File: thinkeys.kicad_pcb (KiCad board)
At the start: 2 copper layers, 363.7 x 279.2 mm, 692 parts, among them J1 Pointing stick, J2 Pointing stick, J3 PWRSWITCH, SW1 SW_Push, SW10 SW_Push, SW11 SW_Push, SW12 SW_Push, SW13 SW_Push, SW14 SW_Push, SW15 SW_Push, SW16 SW_Push, SW17 SW_Push, SW18 SW_Push, SW19 SW_Push, SW2 SW_Push, SW20 SW_Push, SW21 SW_Push, SW22 SW_Push, SW23 SW_Push, SW24 SW_Push, SW25 SW_Push, SW26 SW_Push, SW27 SW_Push, SW28 SW_Push, SW29 SW_Push, SW3 SW_Push, SW30 SW_Push, SW31 SW_Push, SW32 SW_Push, SW33 SW_Push, SW34 SW_Push, SW35 SW_Push, SW36 SW_Push, SW37 SW_Push, SW38 SW_Push, SW39 SW_Push, SW4 SW_Push, SW40 SW_Push, SW41 SW_Push, SW42 SW_Push, SW43 SW_Push, SW44 SW_Push, SW45 SW_Push, SW46 SW_Push, SW47 SW_Push, SW48 SW_Push, SW49 SW_Push, SW5 SW_Push, SW50 SW_Push, SW51 SW_Push, SW52 SW_Push, SW53 SW_Push, SW54 SW_Push, SW55 SW_Push, SW56 SW_Push, SW57 SW_Push, SW58 SW_Push, SW59 SW_Push, SW6 SW_Push, SW60 SW_Push, SW61 SW_Push, SW62 SW_Push, SW63 SW_Push, SW64 SW_Push, SW65 SW_Push, SW66 SW_Push, SW67 SW_Push, SW68 SW_Push, SW69 SW_Push, SW7 SW_Push, SW70 SW_Push, SW71 SW_Push, SW72 SW_Push, SW73 SW_Push, SW74 SW_Push, SW75 SW_Push, SW76 SW_Push, SW77 SW_Push, SW78 SW_Push, SW79 SW_Push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

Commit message: oled btfo
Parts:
- removed OL1, OL2: OLED, libmodulo:128x64OLED

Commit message: switch to matching flush top pad for bottom hole
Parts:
- TP1, TP13, TP14, TP15, TP16, TP17, TP18, TP2, TP25, TP26, TP27, TP28, TP29, TP3, TP30, TP31, TP39, TP4, TP40, TP41, TP42, TP43, TP44, TP45, TP46, TP5, TP55, TP56, TP57, TP58, TP59, TP6, TP65, TP66, TP67, TP68, TP69: footprint libmodulo:TestPoint_Keystone_5019_Minature -> libmodulo:SMDPad_4.0x2.0mm
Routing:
- net /left/c5: track 73.1 -> 75.6 mm
- net /right/r3: track 68.1 -> 70.7 mm
- net /right/c3: track 107.3 -> 109.9 mm
- net /right/c0: track 72.1 -> 74.7 mm
- net /left/r4: track 41.2 -> 43.7 mm
- net /left/r1: track 48.8 -> 51.3 mm
- net /left/c2: track 98.4 -> 101.0 mm
- net /right/c6: track 131.3 -> 133.8 mm
- net VDD: track 64.8 -> 66.0 mm
- net /right/r0: track 161.2 -> 162.5 mm
- net /right/c4: track 115.3 -> 116.6 mm
- net /right/c2: track 96.4 -> 97.6 mm
- net /left/r0: track 135.5 -> 136.8 mm
- net /left/c4: track 79.2 -> 80.5 mm
- net /left/r5: track 38.9 -> 40.1 mm
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
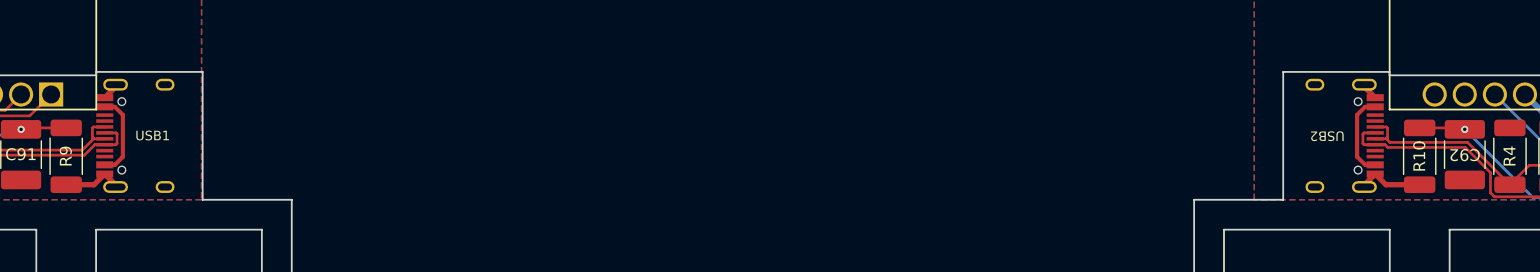
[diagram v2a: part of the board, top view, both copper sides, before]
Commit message: pcb: fix split connection usb location
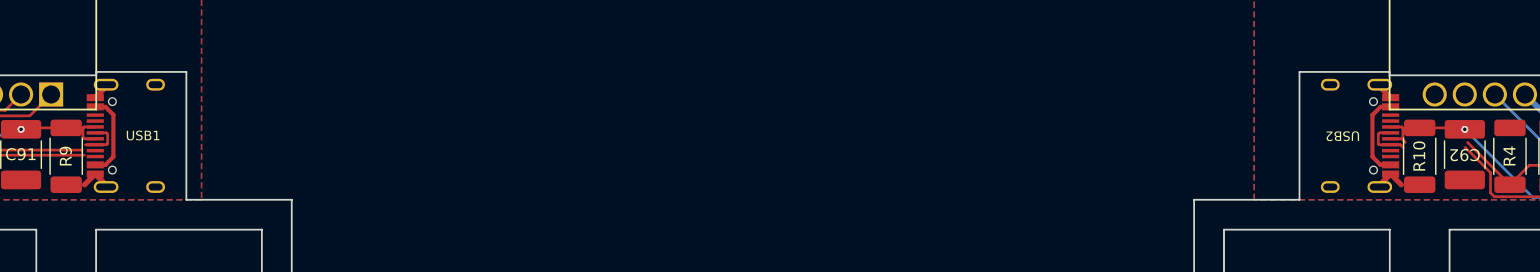
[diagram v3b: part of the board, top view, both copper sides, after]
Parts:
- moved USB2 1.30 mm to (208.9, -14.9)
- moved USB1 0.80 mm to (114.9, -14.9)
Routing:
- net /right/SCL: track 81.1 -> 74.5 mm
- net /right/SDA: track 87.1 -> 80.5 mm
- net GND2: track 49.9 -> 47.0 mm
- net GND1: track 87.9 -> 86.2 mm
- net /left/SDA: track 64.5 -> 63.2 mm
- net /left/SCL: track 57.1 -> 55.8 mm
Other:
- outline, holes or cut-outs redrawn

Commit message: redo top positions, routing & footprints
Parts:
- C91, C92: value 2.2u -> 2.2µ; footprint libmodulo:C_1812_4532Metric_Pad1.57x3.40mm_HandSolder -> Capacitor_SMD:C_1812_4532Metric_Pad1.57x3.40mm_HandSolder
- R1, R10, R2, R3, R4, R5, R6, R7, R8, R9: footprint libmodulo:R_2010_5025Metric_Pad1.40x2.65mm_HandSolder -> Resistor_SMD:R_2010_5025Metric_Pad1.40x2.65mm_HandSolder
- SW91, SW92, SW93: footprint Button_Switch_SMD:SW_SPST_TL3305A -> Button_Switch_SMD:SW_SPST_EVQQ2
- moved SW93 42.8 mm to (286.6, -47.0), turned to 180 degrees
- moved JP2 35.3 mm to (251.5, -48.3), turned to 270 degrees
- moved SW92 15.9 mm to (238.1, -12.7), turned to 180 degrees
- moved SW91 15.3 mm to (85.7, -12.7), turned to 180 degrees
- moved JP1 14.2 mm to (72.4, -13.3), turned to 270 degrees
- moved R3 3.84 mm to (75.6, -12.7)
- moved R1 3.21 mm to (78.7, -12.7)
- moved J3 2.54 mm to (217.8, -33.7)
- moved U1 2.54 mm to (87.0, -26.0)
- moved U2 2.54 mm to (236.9, -26.0)
- moved C91 1.42 mm to (99.7, -12.7)
- moved C92 1.42 mm to (224.2, -12.7), turned to 90 degrees
- moved R10 1.36 mm to (220.3, -12.7), turned to 90 degrees
- moved R4 1.36 mm to (228.0, -12.7)
- moved R9 1.36 mm to (103.5, -12.7)
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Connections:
- U2 pad 1: /right/c7 -> Net-(JP2-Pad3)
- U2 pad 10: /right/c3 -> /right/c4
- U2 pad 11: /right/c2 -> /right/c3
- U2 pad 12: /right/c1 -> /right/c2
- U2 pad 13: /right/c0 -> /right/c1
- U2 pad 14: /right/r1 -> /right/c0
- U2 pad 15: /right/r2 -> /right/r1
- U2 pad 16: Net-(JP2-Pad1) -> /right/r2
- U2 pad 26: Net-(JP2-Pad3) -> Net-(JP2-Pad1)
- U2 pad 7: /right/c6 -> /right/c7
- U2 pad 8: /right/c5 -> /right/c6
- U2 pad 9: /right/c4 -> /right/c5
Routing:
- net Net-(J3-Pad1): track 73.9 -> 0.00 mm
- net GND1: track 86.2 -> 20.3 mm
- net /right/SDA: track 80.5 -> 22.6 mm
- net /right/SCL: track 74.5 -> 18.2 mm
- net /right/DATA: track 72.9 -> 17.2 mm
- net VDD: track 66.0 -> 115.7 mm
- net /left/SDA: track 63.2 -> 16.4 mm
- net Net-(JP1-Pad1): track 18.5 -> 59.9 mm
- net /left/SCL: track 55.8 -> 17.0 mm
- net /right/CLK: track 51.1 -> 25.8 mm
- net /right/RST: track 40.4 -> 15.1 mm, vias 1 -> 0
- net /right/r0: track 162.5 -> 137.6 mm, vias 1 -> 0
- net GND2: track 47.0 -> 24.0 mm, vias 1 -> 0
- net Net-(JP2-Pad3): track 23.0 -> 0.00 mm
- net /right/c7: track 153.7 -> 134.9 mm
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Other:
- outline, holes or cut-outs redrawn

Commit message: pcb: finish routing new top area
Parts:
- JP1, JP2: footprint libmodulo:SolderJumper-3_P1.3mm_Open_RoundedPad1.0x1.5mm_NumberLabels -> Jumper:SolderJumper-3_P1.3mm_Open_RoundedPad1.0x1.5mm_NumberLabels
- moved SW93 45.2 mm to (257.2, -12.7), turned to 0 degrees
- moved JP2 30.2 mm to (255.9, -18.4)
- moved R10 4.44 mm to (224.8, -12.7)
- moved R9 4.44 mm to (99.1, -12.7)
- moved C91 3.18 mm to (102.9, -12.7)
- moved C92 3.18 mm to (221.0, -12.7)
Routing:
- net Net-(J3-Pad1): track 0.00 -> 108.9 mm
- net GND1: track 20.3 -> 100.5 mm
- net /right/DATA: track 17.2 -> 95.4 mm
- net /right/SDA: track 22.6 -> 85.3 mm
- net GND2: track 24.0 -> 86.5 mm, vias 0 -> 1
- net /right/SCL: track 18.2 -> 80.1 mm
- net Net-(JP2-Pad3): track 0.00 -> 52.3 mm
- net VCC: track 68.7 -> 105.2 mm
- net /left/RST: track 40.7 -> 75.7 mm
- net /left/SCL: track 17.0 -> 50.2 mm
- net /right/CLK: track 25.8 -> 58.2 mm
- net /left/SDA: track 16.4 -> 45.3 mm
- net /right/r0: track 137.6 -> 161.2 mm, vias 0 -> 1
- net Net-(JP1-Pad3): track 1.89 -> 13.6 mm
- net Net-(JP2-Pad1): track 0.00 -> 11.1 mm, vias 0 -> 1
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
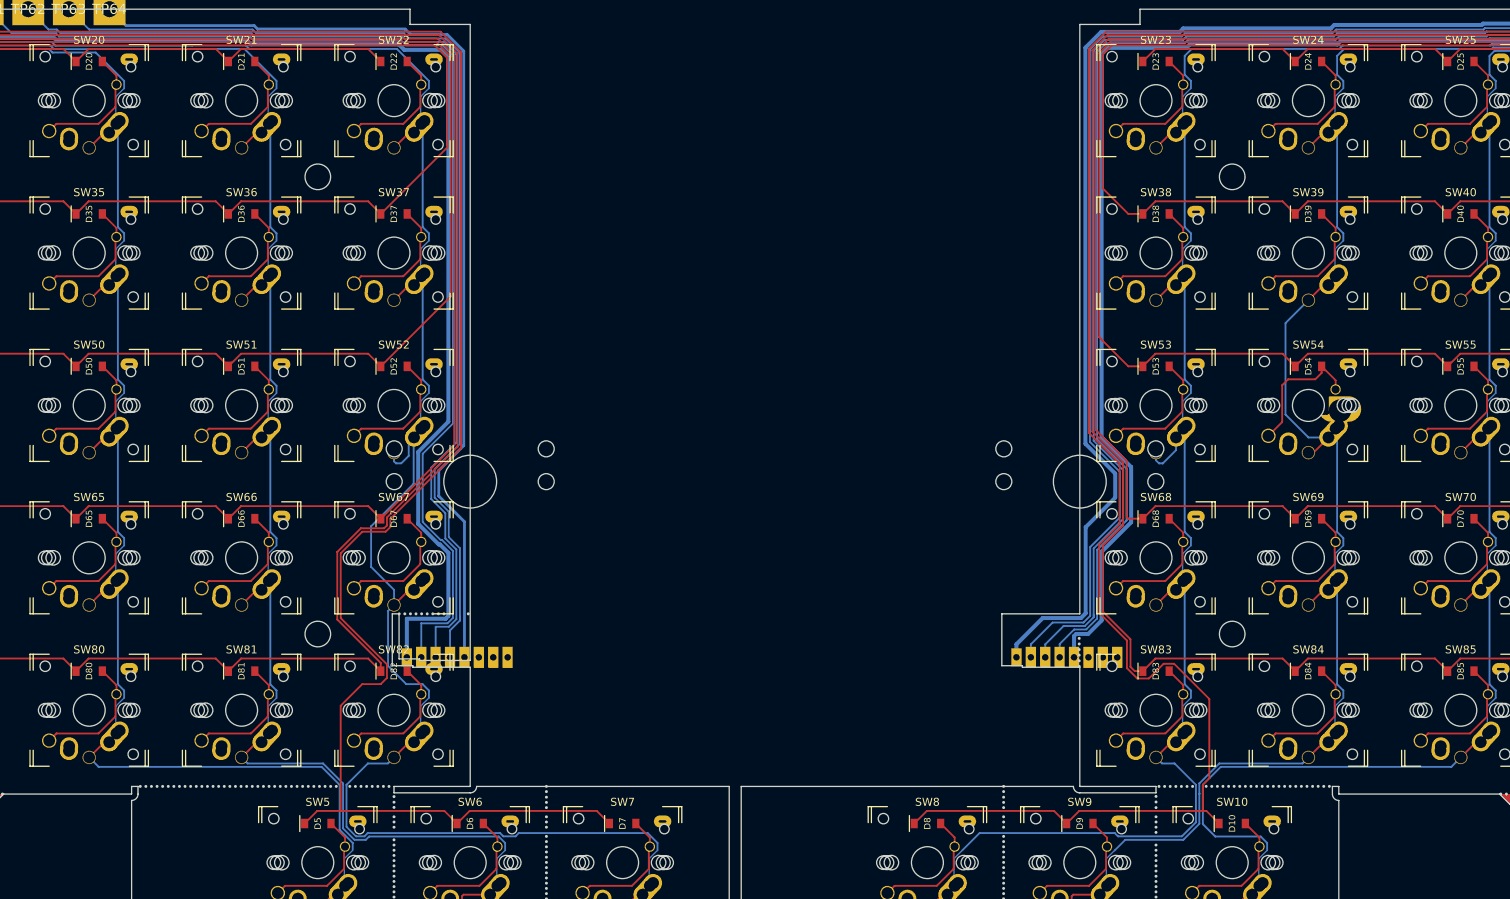
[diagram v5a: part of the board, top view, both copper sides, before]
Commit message: pcb: add magnetic tenting kit support
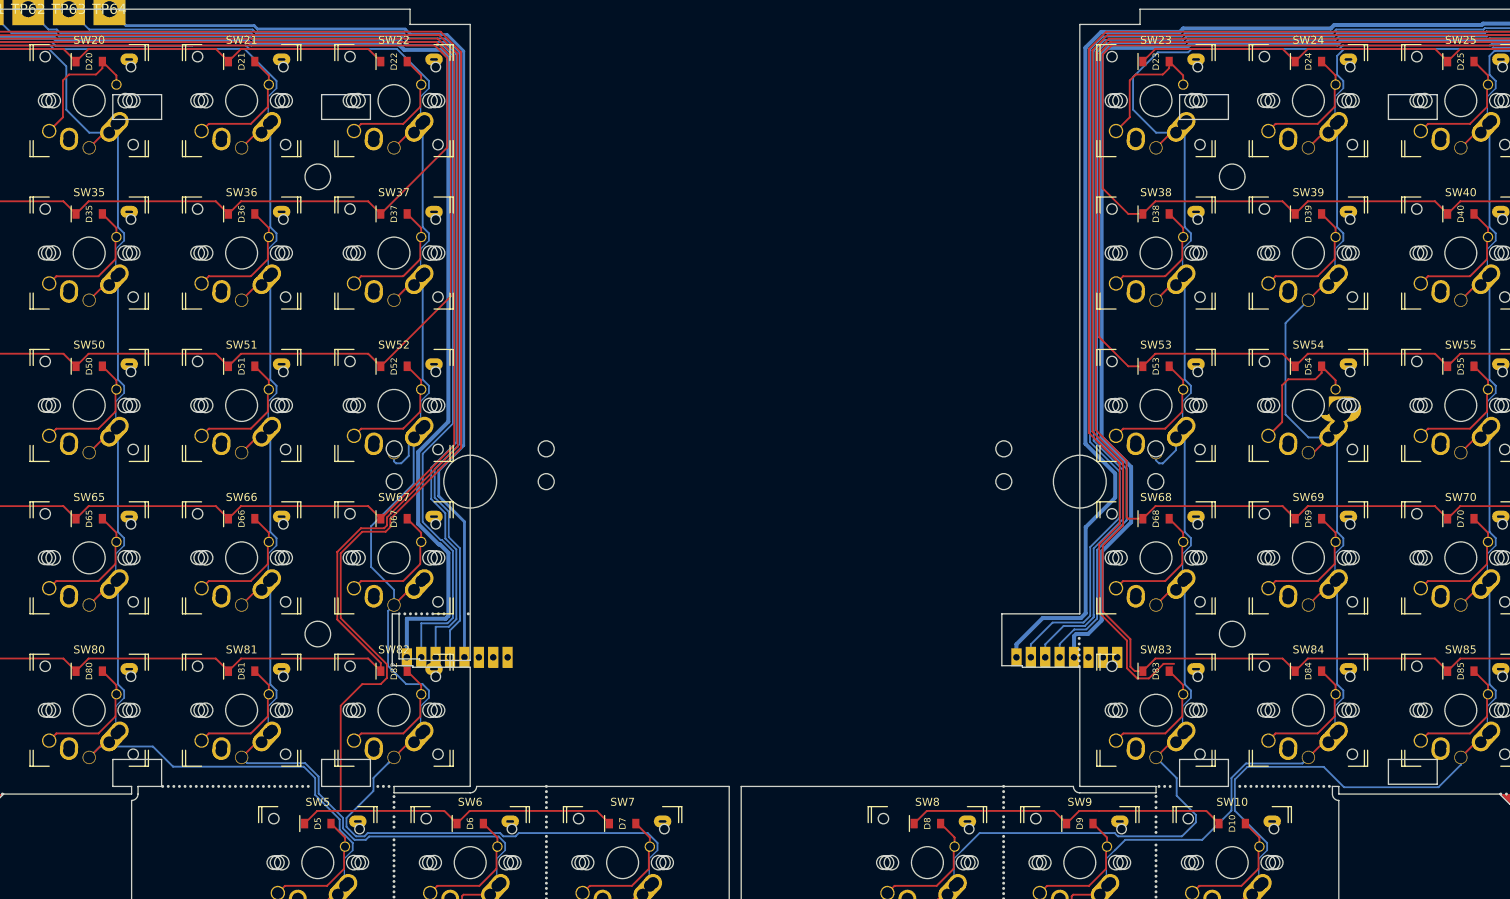
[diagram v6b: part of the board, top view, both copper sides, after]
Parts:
- removed the ? at (84.7, 219.1)
- removed the ? at (83.3, 219.1)
- removed the ? at (107.1, 219.1)
- removed the ? at (109.5, 219.1)
- removed the ? at (110.2, 219.1)
- removed the ? at (219.3, 219.1)
- removed the ? at (217.9, 219.1)
- removed the ? at (108.8, 219.1)
- removed the ? at (217.2, 219.1)
- removed the ? at (110.9, 219.1)
- removed the ? at (218.6, 219.1)
- removed the ? at (104.3, 219.1)
- removed the ? at (111.6, 219.1)
- removed the ? at (105.7, 219.1)
- removed the ? at (105.0, 219.1)
- removed the ? at (84.0, 219.1)
- removed the ? at (216.5, 219.1)
- removed the ? at (215.8, 219.1)
- removed the ? at (212.7, 219.1)
- removed the ? at (213.4, 219.1)
- removed the ? at (214.1, 219.1)
- removed the ? at (212.0, 219.1)
- removed the ? at (82.6, 219.1)
- removed the ? at (106.4, 219.1)
- added REF**: Magnetic Tenting Kit, libmodulo:Magnetic_Tenting_Kit, F.Cu at (228.6, 175.7)
- added REF**: Magnetic Tenting Kit, libmodulo:Magnetic_Tenting_Kit, F.Cu at (95.2, 175.7)
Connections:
- Ref** pad : (no net) -> Net-(SW21-Pad2)
- Ref** pad : (no net) -> Net-(SW24-Pad2)
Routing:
- net Net-(D10-Pad1): track 234.8 -> 214.2 mm
- net Net-(SW23-Pad2): track 260.7 -> 268.4 mm
- net Net-(SW10-Pad2): track 237.3 -> 231.4 mm
- net Net-(SW20-Pad2): track 220.8 -> 218.6 mm
- net Net-(SW21-Pad2): track 238.2 -> 236.9 mm
- net Net-(D23-Pad2): track 15.8 -> 17.0 mm
- net Net-(D20-Pad2): track 15.8 -> 17.0 mm
- net Net-(SW24-Pad2): track 239.5 -> 238.9 mm

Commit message: move trackpoint
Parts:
- removed the ? at (199.9, 203.4)
- removed the ? at (117.8, 197.5)
- removed the ? at (119.2, 197.5)
- removed the ? at (123.6, 197.5)
- removed the ? at (115.7, 197.5)
- removed the ? at (116.3, 197.5)
- removed the ? at (119.8, 197.5)
- removed the ? at (120.5, 197.5)
- removed the ? at (199.9, 200.6)
- removed the ? at (199.9, 204.1)
- removed the ? at (117.0, 197.5)
- removed the ? at (118.5, 197.5)
- removed the ? at (115.0, 197.5)
- removed the ? at (199.9, 202.7)
- removed the ? at (199.9, 202.0)
- removed the ? at (199.9, 201.3)
- removed D52, D53, D67, D68: D, libmodulo:D_SOD-123
- removed the REF** at (209.6, 57.1)
- removed the REF** at (209.6, 38.1)
- removed the REF** at (114.3, 38.1)
- removed the REF** at (200.0, 47.6)
- removed the REF** at (114.3, 57.1)
- removed the REF** at (123.8, 47.6)
- removed SW52, SW53, SW67, SW68: SW_Push, libmodulo:SW_MX-ALPS-ChocV1_V2-X-PG1280_PCB
- removed TP55, TP65: GND, libmodulo:SMDPad_4.0x2.0mm
- removed TP56, TP66: DATA, libmodulo:SMDPad_4.0x2.0mm
- removed TP57, TP67: CLK, libmodulo:SMDPad_4.0x2.0mm
- removed TP58, TP68: RST, libmodulo:SMDPad_4.0x2.0mm
- removed TP59, TP69: VCC, libmodulo:SMDPad_4.0x2.0mm
- removed TP60, TP70: GND, libmodulo:THTPad_4.0x4.0mm_Drill2.0mm
- removed TP61, TP71: DATA, libmodulo:THTPad_4.0x4.0mm_Drill2.0mm
- removed TP62, TP72: CLK, libmodulo:THTPad_4.0x4.0mm_Drill2.0mm
- removed TP63, TP73: RST, libmodulo:THTPad_4.0x4.0mm_Drill2.0mm
- removed TP64, TP74: VCC, libmodulo:THTPad_4.0x4.0mm_Drill2.0mm
- added REF**: SK8707-01, libmodulo:SK8707-01-cutout, F.Cu at (211.5, 171.8)
- added REF**: SK8707-01, libmodulo:SK8707-01-cutout, F.Cu at (112.3, 171.8)
- JP1, JP2: footprint Jumper:SolderJumper-3_P1.3mm_Open_RoundedPad1.0x1.5mm_NumberLabels -> libmodulo:SolderJumper-3_P1.3mm_Open_RoundedPad1.0x1.5mm_NumberLabels
- moved J1 142.9 mm to (112.3, 38.5)
- moved J2 142.9 mm to (211.5, 38.5)
- moved TP5 25.4 mm to (27.9, -11.4)
- moved TP6 25.4 mm to (53.3, -11.4)
- moved TP7 25.4 mm to (27.9, 121.9)
- moved TP8 25.4 mm to (53.3, 121.9)
- moved TP13 25.4 mm to (309.9, -11.4)
- moved TP18 25.4 mm to (284.5, -11.4)
- moved TP19 25.4 mm to (309.9, 121.9)
- moved TP20 25.4 mm to (284.5, 121.9)
- moved TP14 15.2 mm to (304.8, -11.4)
- moved TP17 15.2 mm to (289.6, -11.4)
- moved TP21 15.2 mm to (289.6, 121.9)
- moved TP24 15.2 mm to (304.8, 121.9)
- moved TP1 15.2 mm to (48.3, -11.4)
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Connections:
- J1 pad 1: Net-(J1-Pad1) -> GND1
- J1 pad 2: Net-(J1-Pad2) -> /left/DATA
- J1 pad 3: Net-(J1-Pad3) -> /left/CLK
- J1 pad 4: Net-(J1-Pad4) -> Net-(C91-Pad1)
- J1 pad 5: Net-(J1-Pad5) -> VCC
- J2 pad 1: Net-(J2-Pad1) -> GND2
- J2 pad 2: Net-(J2-Pad2) -> /right/DATA
- J2 pad 3: Net-(J2-Pad3) -> /right/CLK
- J2 pad 4: Net-(J2-Pad4) -> Net-(C92-Pad1)
- J2 pad 5: Net-(J2-Pad5) -> VDD
- U1 pad 10: /left/r2 -> /left/r3
- U1 pad 11: /left/r1 -> /left/r4
- U1 pad 12: /left/r0 -> /left/r5
- U1 pad 7: /left/r5 -> /left/r0
- U1 pad 8: /left/r4 -> /left/r1
- U1 pad 9: /left/r3 -> /left/r2
- U2 pad 15: /right/r1 -> /right/r0
- U2 pad 16: /right/r2 -> /right/r5
- U2 pad 17: /right/r3 -> /right/r4
- U2 pad 18: /right/r4 -> /right/r3
- U2 pad 19: /right/r5 -> /right/r2
- U2 pad 20: /right/r0 -> /right/r1
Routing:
- net Net-(J2-Pad5): track 159.0 -> 0.00 mm
- net Net-(J2-Pad4): track 155.3 -> 0.00 mm
- net Net-(J2-Pad3): track 152.3 -> 0.00 mm
- net Net-(J2-Pad2): track 148.8 -> 0.00 mm
- net Net-(J1-Pad1): track 147.3 -> 0.00 mm
- net Net-(J2-Pad1): track 145.1 -> 0.00 mm
- net Net-(J1-Pad2): track 141.9 -> 0.00 mm
- net Net-(J1-Pad3): track 135.3 -> 0.00 mm
- net Net-(J1-Pad4): track 129.8 -> 0.00 mm
- net Net-(J1-Pad5): track 124.0 -> 0.00 mm
- net Net-(D10-Pad1): track 214.2 -> 312.7 mm
- net VCC: track 105.2 -> 193.8 mm
- net /left/CLK: track 37.6 -> 124.2 mm
- net /right/DATA: track 95.4 -> 181.0 mm
- net GND2: track 86.5 -> 166.6 mm
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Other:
- outline, holes or cut-outs redrawn

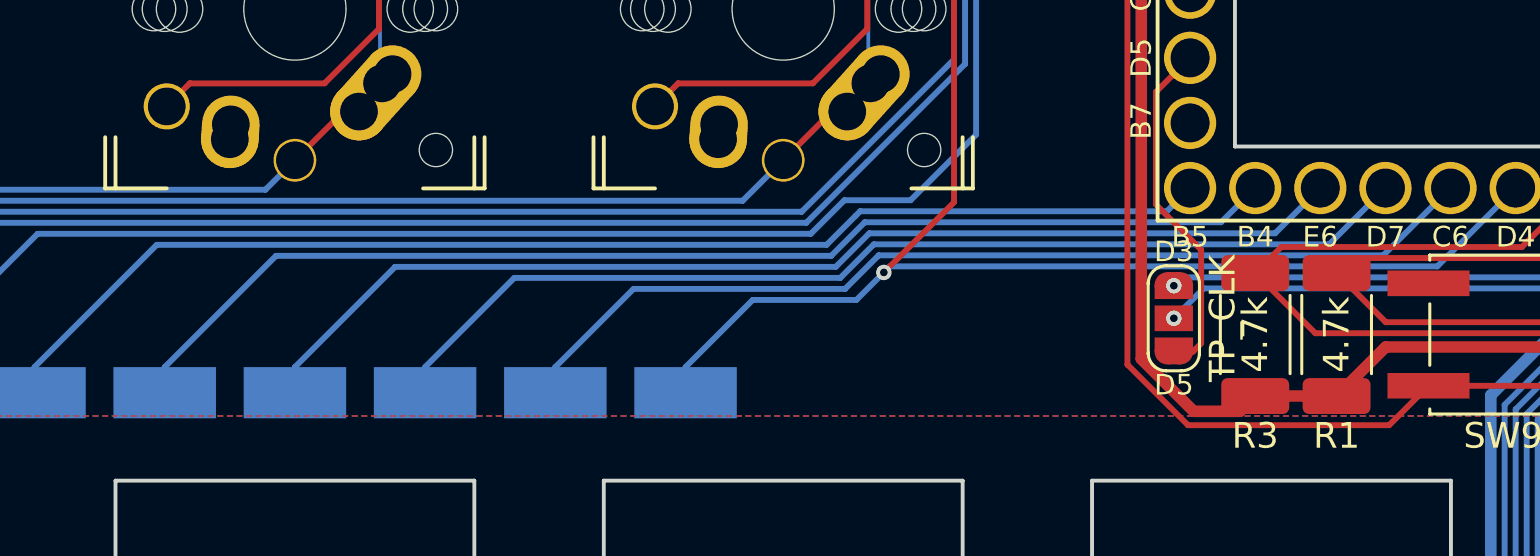
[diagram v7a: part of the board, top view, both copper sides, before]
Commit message: fix left side row pin positions
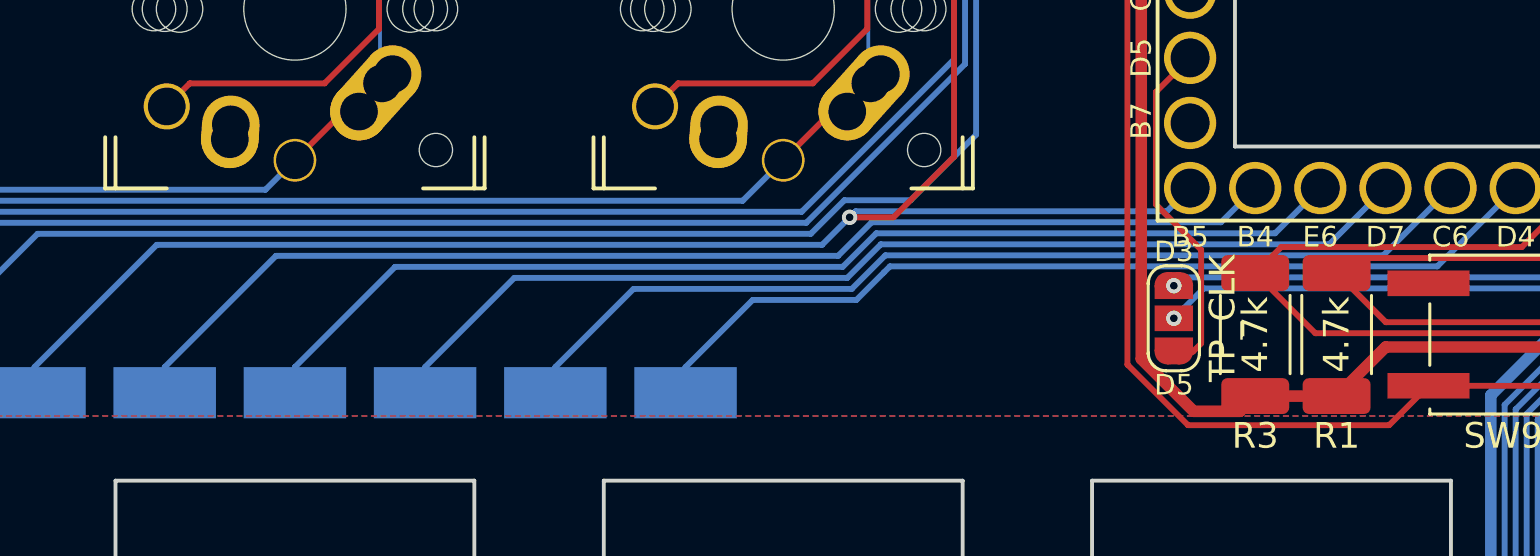
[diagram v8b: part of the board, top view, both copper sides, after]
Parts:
- moved TP6 25.4 mm to (27.9, -11.4)
- moved TP1 5.08 mm to (53.3, -11.4)
- moved TP5 5.08 mm to (33.0, -11.4)
- moved TP2 5.08 mm to (48.3, -11.4)
- moved TP3 5.08 mm to (43.2, -11.4)
- moved TP4 5.08 mm to (38.1, -11.4)
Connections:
- U1 pad 10: /left/r3 -> /left/r4
- U1 pad 11: /left/r4 -> /left/r5
- U1 pad 12: /left/r5 -> /left/r0
- U1 pad 7: /left/r0 -> /left/r1
- U1 pad 8: /left/r1 -> /left/r2
- U1 pad 9: /left/r2 -> /left/r3
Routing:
- net /left/r0: track 123.8 -> 135.9 mm
- net /left/r4: track 48.0 -> 44.2 mm
- net /left/r3: track 44.2 -> 41.6 mm
- net /left/r5: track 49.2 -> 46.7 mm
- net /left/r1: track 40.4 -> 37.8 mm
- net /left/r2: track 41.6 -> 39.1 mm
